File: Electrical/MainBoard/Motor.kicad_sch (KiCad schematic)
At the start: 0 parts

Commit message: Add more schematics and begin floorplanning
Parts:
- added C1 (x2): 0.01 uF, Capacitor_SMD:C_0805_2012Metric_Pad1.18x1.45mm_HandSolder, symbol Device:C
- added C2 (x2), C4 (x2), C5 (x4): 0.1 uF, Capacitor_SMD:C_0805_2012Metric_Pad1.18x1.45mm_HandSolder, symbol Device:C
- added C3 (x2): 100 uF, RobotLibrary:PCAP_8x10-ELECT_NCA-M, symbol Device:C_Polarized_US
- added C6 (x2): 0.47 uF, Capacitor_SMD:C_0805_2012Metric_Pad1.18x1.45mm_HandSolder, symbol Device:C
- added M1 (x2): Motor_DC, RobotLibrary:CONN_1890963_PXC, symbol Motor:Motor_DC
- added R1 (x2): 0.25R, Resistor_SMD:R_0805_2012Metric_Pad1.20x1.40mm_HandSolder, symbol Device:R_US
- added R10 (x2): 51k, Resistor_SMD:R_0805_2012Metric_Pad1.20x1.40mm_HandSolder, symbol Device:R_US
- added R2 (x2): 1M, Resistor_SMD:R_0805_2012Metric_Pad1.20x1.40mm_HandSolder, symbol Device:R_US
- added R3 (x2), R4 (x2), R5 (x2), R6 (x2), R7 (x2): 0R, Resistor_SMD:R_0805_2012Metric_Pad1.20x1.40mm_HandSolder, symbol Device:R_US
- added R8 (x2): 10k, Resistor_SMD:R_0805_2012Metric_Pad1.20x1.40mm_HandSolder, symbol Device:R_US
- added R9 (x2): 16k, Resistor_SMD:R_0805_2012Metric_Pad1.20x1.40mm_HandSolder, symbol Device:R_US
- added U1 (x2): DRV8842PWPR, RobotLibrary:PWP0028C_M, symbol Matts_Library:DRV8842PWPR
- added U13, U14: Quad_Encoder, RobotLibrary:CONN_22-23-2041_MOL, symbol RobotLibary:Quadrature_Encoder
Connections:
- net GND: now also C2.2, C2.2, C3.2, C3.2, C4.2, C4.2, C5.2, C5.2, C6.2, C6.2, R1.1, R1.1, R10.2, R10.2, U1.14 (GND), U1.14 (GND), U1.28 (GND), U1.28 (GND), U1.29 (PAD), U1.29 (PAD), U13.4 (GND), U14.4 (GND)
- net IC1: now also U13.1 (PhaseA)
- net IC2: now also U13.2 (PhaseB)
- net IC3: now also U14.1 (PhaseA)
- net IC4: now also U14.2 (PhaseB)
- net OC1: now also U1.21 (IN1)
- net OC2: now also U1.21 (IN1)
- net Vdrive: now also C2.1, C2.1, C3.1, C3.1, C4.1, C4.1, C5.2, C5.2, R2.1, R2.1, U1.11 (VM), U1.11 (VM), U1.4 (VM), U1.4 (VM)
- new net: C5.1, R2.2, U1.3 (VCP) (x2)
- new net: M1.1 (+), U1.10 (OUT1), U1.5 (OUT1) (x2)
- new net: M1.2 (-), U1.7 (OUT2), U1.8 (OUT2) (x2)
- new net: C6.1, R8.2, R9.1, U1.15 (V3P3OUT) (x2)
- new net: R5.2, U1.25 (I2) (x2)
- new net: C1.1, U1.1 (CP1) (x2)
- new net: C1.2, U1.2 (CP2) (x2)
- new net: R3.2, U1.23 (I0) (x2)
- new net: R10.1, R9.2, U1.12 (VREF), U1.13 (VREF) (x2)
- new net: R4.2, U1.24 (I1) (x2)
- new net: R6.2, U1.26 (I3) (x2)
- new net: R7.2, U1.27 (I4) (x2)
- new net +3.3V: C5.1, C5.1, R3.1, R3.1, R4.1, R4.1, R5.1, R5.1, R6.1, R6.1, R7.1, R7.1, U1.16 (RESET_N), U1.16 (RESET_N), U1.17 (SLEEP_N), U1.17 (SLEEP_N), U13.3 (Vcc), U14.3 (Vcc)
- new net Dir1: U1.20 (IN2)
- new net Dir2: U1.20 (IN2)
- new net Fault1: R8.1, U1.18 (FAULT_N)
- new net Fault2: R8.1, U1.18 (FAULT_N)
- new net MotorCurrent1: R1.2, U1.6 (ISEN), U1.9 (ISEN)
- new net MotorCurrent2: R1.2, U1.6 (ISEN), U1.9 (ISEN)
- no-connect marks 0 -> 4
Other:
- note added: "5 A Max Continuous Current"
- note added: "Chopping Current at 100% Scale"
- note added: "Corresponding Female: DigiKey PN WM2002-ND Corresponding Crimp : DigiKey PN WM2756CT-ND"
- note added: "Current Sensing Resistor Surface Mount Low Inductance Rated for high enough power: Irms^2 * R Placed close to motor driver"
- note added: "Fault"
- note added: "I0 - I4 Function"
- note added: "Motor Voltage: 8.2 V min 45 V max"
- note added: "PWM Frequency: 100 kHz max"
- note added: "Signal Conditioning?"
- note added: "Slow Decay: Logic low Mixed Decay: Open Fast Decay: Logic high"
- note added: "VREF Voltage: 1 V min 3.5 V max"

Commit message: Begin layout of pcb
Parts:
- renumbered U14 to U11, U13 to U12

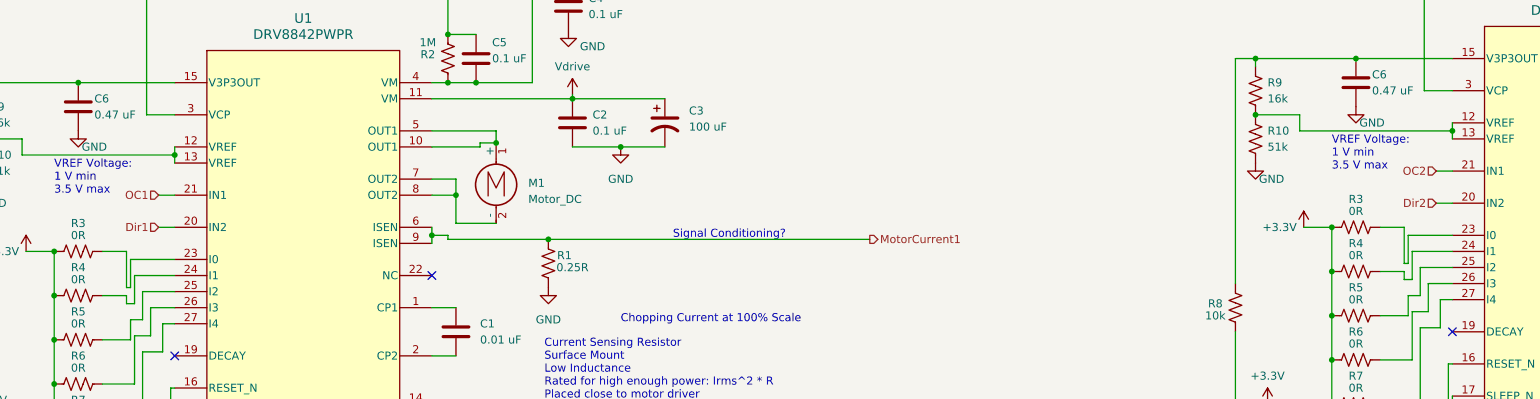
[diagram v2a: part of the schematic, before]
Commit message: First Pass at the routing
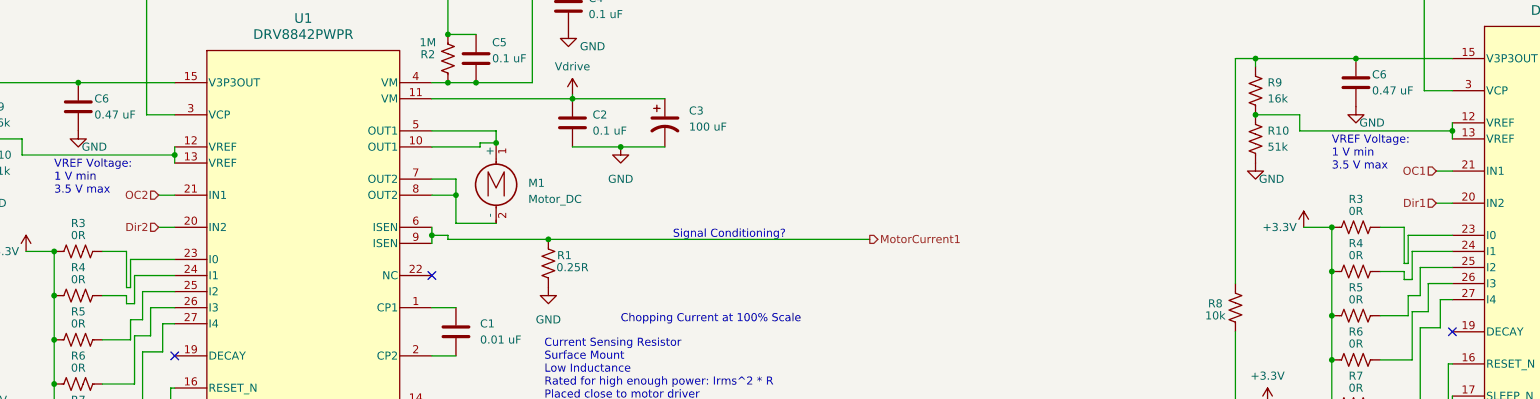
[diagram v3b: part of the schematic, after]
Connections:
- net Dir1: now also U1.20 (IN2); no longer U1.20 (IN2)
- net Dir2: now also U1.20 (IN2); no longer U1.20 (IN2)
- net OC1: now also U1.21 (IN1); no longer U1.21 (IN1)
- net OC2: now also U1.21 (IN1); no longer U1.21 (IN1)
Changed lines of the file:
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@@
     (effects (font (size 1.27 1.27)) (justify left))
+  )
+  (hierarchical_label "OC2" (shape input) (at 78.105 83.185 180) (fields_autoplaced)
+    (effects (font (size 1.27 1.27)) (justify right))
   )
   (hierarchical_label "IC1" (shape output) (at 263.525 179.07 180) (fields_autoplaced)
@@
     (effects (font (size 1.27 1.27)) (justify right))
   )
-  (hierarchical_label "Dir1" (shape input) (at 78.105 88.265 180) (fields_autoplaced)
-    (effects (font (size 1.27 1.27)) (justify right))
-  )
-  (hierarchical_label "Dir2" (shape input) (at 280.035 84.455 180) (fields_autoplaced)
+  (hierarchical_label "OC1" (shape input) (at 280.035 79.375 180) (fields_autoplaced)
     (effects (font (size 1.27 1.27)) (justify right))
   )
@@
     (effects (font (size 1.27 1.27)) (justify right))
   )
-  (hierarchical_label "OC1" (shape input) (at 78.105 83.185 180) (fields_autoplaced)
+  (hierarchical_label "Dir2" (shape input) (at 78.105 88.265 180) (fields_autoplaced)
     (effects (font (size 1.27 1.27)) (justify right))
   )
@@
     (effects (font (size 1.27 1.27)) (justify right))
   )
+  (hierarchical_label "Dir1" (shape input) (at 280.035 84.455 180) (fields_autoplaced)
+    (effects (font (size 1.27 1.27)) (justify right))
+  )
   (hierarchical_label "GND" (shape output) (at 294.005 256.54 180) (fields_autoplaced)
     (effects (font (size 1.27 1.27)) (justify right))
   )
-  (hierarchical_label "OC2" (shape input) (at 280.035 79.375 180) (fields_autoplaced)
-    (effects (font (size 1.27 1.27)) (justify right))
-  )

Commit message: Add some finishing touches and create preliminary boms
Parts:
- removed C2 (x2), C5 (x2): 0.1 uF, Capacitor_SMD:C_0805_2012Metric_Pad1.18x1.45mm_HandSolder, symbol Device:C
- removed R4 (x2), R5 (x2), R6 (x2), R7 (x2): 0R, Resistor_SMD:R_0805_2012Metric_Pad1.20x1.40mm_HandSolder, symbol Device:R_US
- added C4 (x4): 0.1 uF, Capacitor_SMD:C_0805_2012Metric_Pad1.18x1.45mm_HandSolder, symbol Device:C
- added R3 (x8): 0R, Resistor_SMD:R_0805_2012Metric_Pad1.20x1.40mm_HandSolder, symbol Device:R_US
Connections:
- net +3.3V: now also R3.1, R3.1, R3.1, R3.1, R3.1, R3.1, R3.1, R3.1
- net GND: now also C4.2, C4.2
- net Vdrive: now also C4.1, C4.1, C4.1, C4.2
- net at R2.2, U1.3 (VCP): now also C4.1
- net at R2.2, U1.3 (VCP): now also C4.2
- net at U1.25 (I2): now also R3.2 (x2)
- net at U1.24 (I1): now also R3.2 (x2)
- net at U1.26 (I3): now also R3.2 (x2)
- net at U1.27 (I4): now also R3.2 (x2)

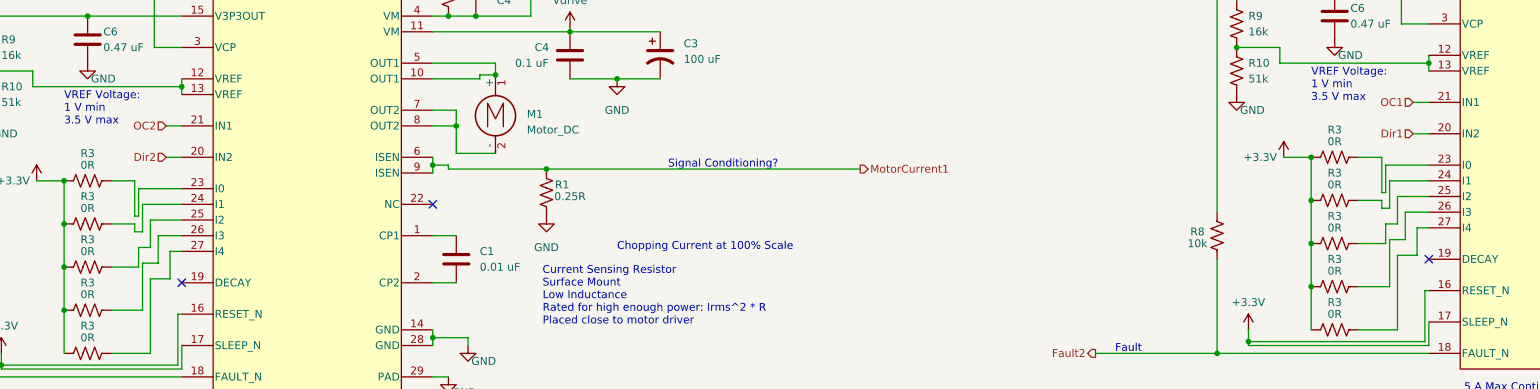
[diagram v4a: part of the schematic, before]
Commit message: Finish final board design for Rev 0.1 Main board and reflective Sensor. Created Gerbers.
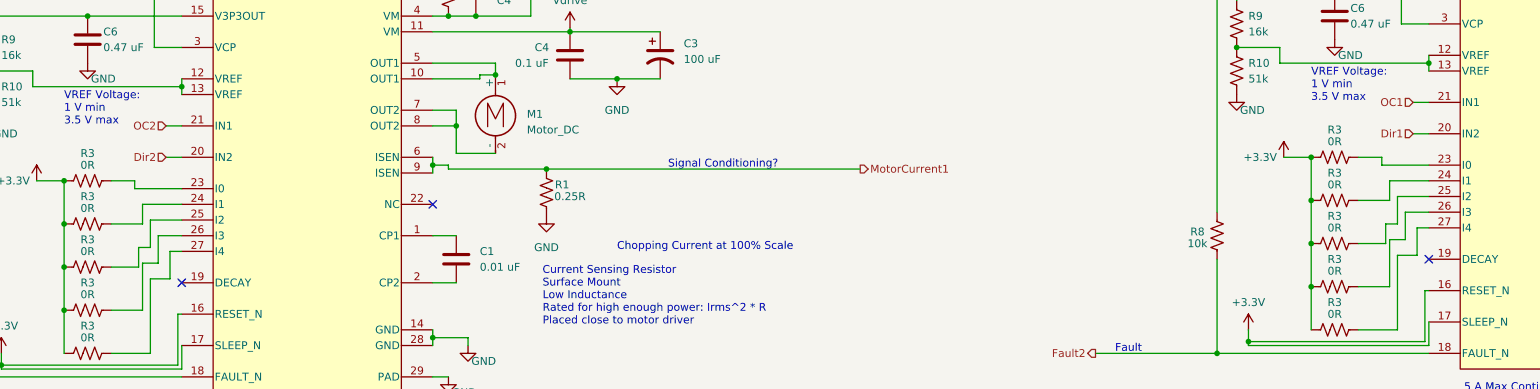
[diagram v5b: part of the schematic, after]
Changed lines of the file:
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@@
     (stroke (width 0) (type default))
   )
-  (wire (pts (xy 274.955 93.98) (xy 274.955 88.265))
+  (wire (pts (xy 274.955 89.535) (xy 274.955 88.265))
     (stroke (width 0) (type default))
   )
@@
     (stroke (width 0) (type default))
   )
-  (wire (pts (xy 73.025 97.79) (xy 73.025 92.075))
+  (wire (pts (xy 73.025 93.345) (xy 73.025 92.075))
     (stroke (width 0) (type default))
   )
@@
     (stroke (width 0) (type default))
   )
-  (wire (pts (xy 69.215 99.06) (xy 73.025 99.06))
-    (stroke (width 0) (type default))
-  )
   (wire (pts (xy 75.565 107.95) (xy 75.565 120.015))
     (stroke (width 0) (type default))
@@
     (stroke (width 0) (type default))
   )
-  (wire (pts (xy 73.025 99.06) (xy 73.025 100.33))
-    (stroke (width 0) (type default))
-  )
   (wire (pts (xy 75.565 98.425) (xy 80.645 98.425))
     (stroke (width 0) (type default))
@@
     (stroke (width 0) (type default))
   )
-  (wire (pts (xy 73.66 93.345) (xy 80.645 93.345))
-    (stroke (width 0) (type default))
-  )
-  (wire (pts (xy 275.59 89.535) (xy 282.575 89.535))
+  (wire (pts (xy 274.955 89.535) (xy 282.575 89.535))
     (stroke (width 0) (type default))
   )
@@
     (stroke (width 0) (type default))
   )
-  (wire (pts (xy 275.59 93.98) (xy 274.955 93.98))
-    (stroke (width 0) (type default))
-  )
   (wire (pts (xy 281.94 109.855) (xy 282.575 109.855))
     (stroke (width 0) (type default))
@@
     (stroke (width 0) (type default))
   )
-  (wire (pts (xy 74.295 100.33) (xy 74.295 95.885))
+  (wire (pts (xy 74.295 99.06) (xy 74.295 95.885))
     (stroke (width 0) (type default))
   )
@@
     (stroke (width 0) (type default))
   )
-  (wire (pts (xy 73.66 97.79) (xy 73.025 97.79))
+  (wire (pts (xy 73.025 93.345) (xy 80.645 93.345))
     (stroke (width 0) (type default))
   )
@@
     (stroke (width 0) (type default))
   )
-  (wire (pts (xy 73.025 100.33) (xy 74.295 100.33))
+  (wire (pts (xy 69.215 99.06) (xy 74.295 99.06))
     (stroke (width 0) (type default))
   )
@@
     (stroke (width 0) (type default))
   )
-  (wire (pts (xy 275.59 93.98) (xy 275.59 89.535))
-    (stroke (width 0) (type default))
-  )
   (wire (pts (xy 325.755 53.975) (xy 325.755 48.26))
     (stroke (width 0) (type default))
@@
     (stroke (width 0) (type default))
   )
-  (wire (pts (xy 271.145 95.25) (xy 274.955 95.25))
-    (stroke (width 0) (type default))
-  )
   (wire (pts (xy 327.025 83.82) (xy 333.375 83.82))
     (stroke (width 0) (type default))
@@
     (stroke (width 0) (type default))
   )
-  (wire (pts (xy 73.66 97.79) (xy 73.66 93.345))
-    (stroke (width 0) (type default))
-  )
   (wire (pts (xy 142.875 49.53) (xy 137.16 49.53))
     (stroke (width 0) (type default))
@@
     (stroke (width 0) (type default))
   )
-  (wire (pts (xy 274.955 96.52) (xy 276.225 96.52))
+  (wire (pts (xy 271.145 95.25) (xy 276.225 95.25))
     (stroke (width 0) (type default))
   )
@@
     (stroke (width 0) (type default))
   )
-  (wire (pts (xy 276.225 96.52) (xy 276.225 92.075))
+  (wire (pts (xy 276.225 95.25) (xy 276.225 92.075))
     (stroke (width 0) (type default))
   )
@@
     (stroke (width 0) (type default))
   )
-  (wire (pts (xy 274.955 95.25) (xy 274.955 96.52))
-    (stroke (width 0) (type default))
-  )

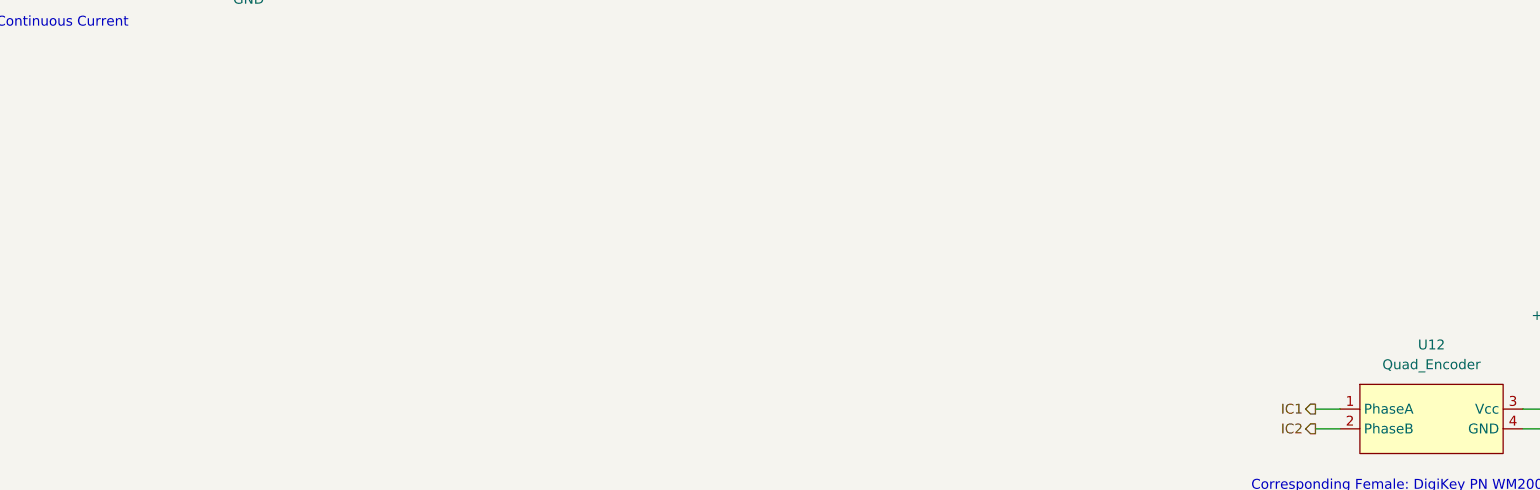
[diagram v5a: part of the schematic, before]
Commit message: Add comments to schematic for future revs
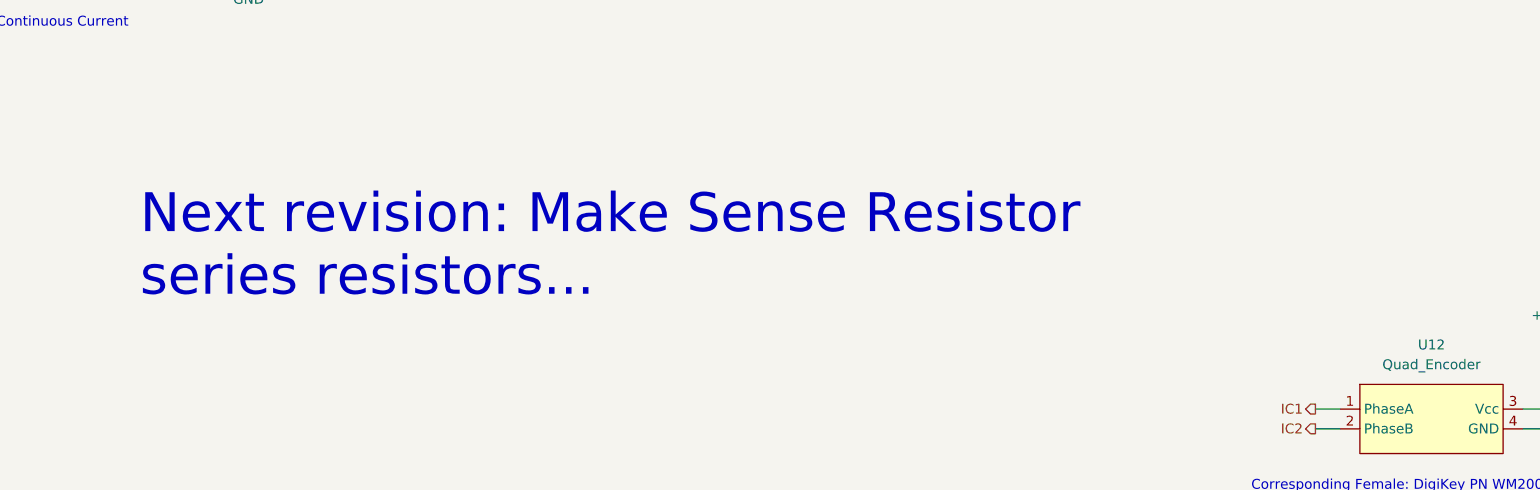
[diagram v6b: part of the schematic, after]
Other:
- note added: "Next revision: Make Sense Resistor series resistors..."
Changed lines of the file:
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@@
     (effects (font (size 1.27 1.27)) (justify left bottom))
+  )
+  (text "Next revision: Make Sense Resistor\nseries resistors..."
+    (at 112.395 165.1 0)
+    (effects (font (size 5 5)) (justify left bottom))
   )
   (text "Motor Voltage:\n8.2 V min\n45 V max" (at 348.615 45.085 0)

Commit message: Made V0.2 revisions to Main Board
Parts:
- removed R1: 0.25R, Resistor_SMD:R_0805_2012Metric_Pad1.20x1.40mm_HandSolder, symbol Device:R_US
- added R1 (x3): 0.1R, Resistor_SMD:R_0603_1608Metric_Pad0.98x0.95mm_HandSolder, symbol Device:R_US
- added R1 (x2): 0.05 R, Resistor_SMD:R_0603_1608Metric_Pad0.98x0.95mm_HandSolder, symbol Device:R_US
- R1: value 0.25R -> 0.1R; footprint Resistor_SMD:R_0805_2012Metric_Pad1.20x1.40mm_HandSolder -> Resistor_SMD:R_0603_1608Metric_Pad0.98x0.95mm_HandSolder; Mfr Stackpole Electronics Inc -> Panasonic Electronic Components; Mfr P/N CSR0805FKR250 -> ERJ-6DSJR10V; Supplier 1 P/N CSR0805FKR250CT-ND -> P19260CT-ND
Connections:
- net GND: now also R1.1, R1.1; no longer R1.1
- net MotorCurrent2: now also R1.2
- new net: R1.1, R1.2 (x4)
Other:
- note removed: "Next revision: Make Sense Resistor series resistors..."
- note removed: "Signal Conditioning?"
